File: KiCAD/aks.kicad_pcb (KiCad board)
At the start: 2 copper layers, 30 x 35 mm, 40 parts, among them M3 ОтверстиеD3

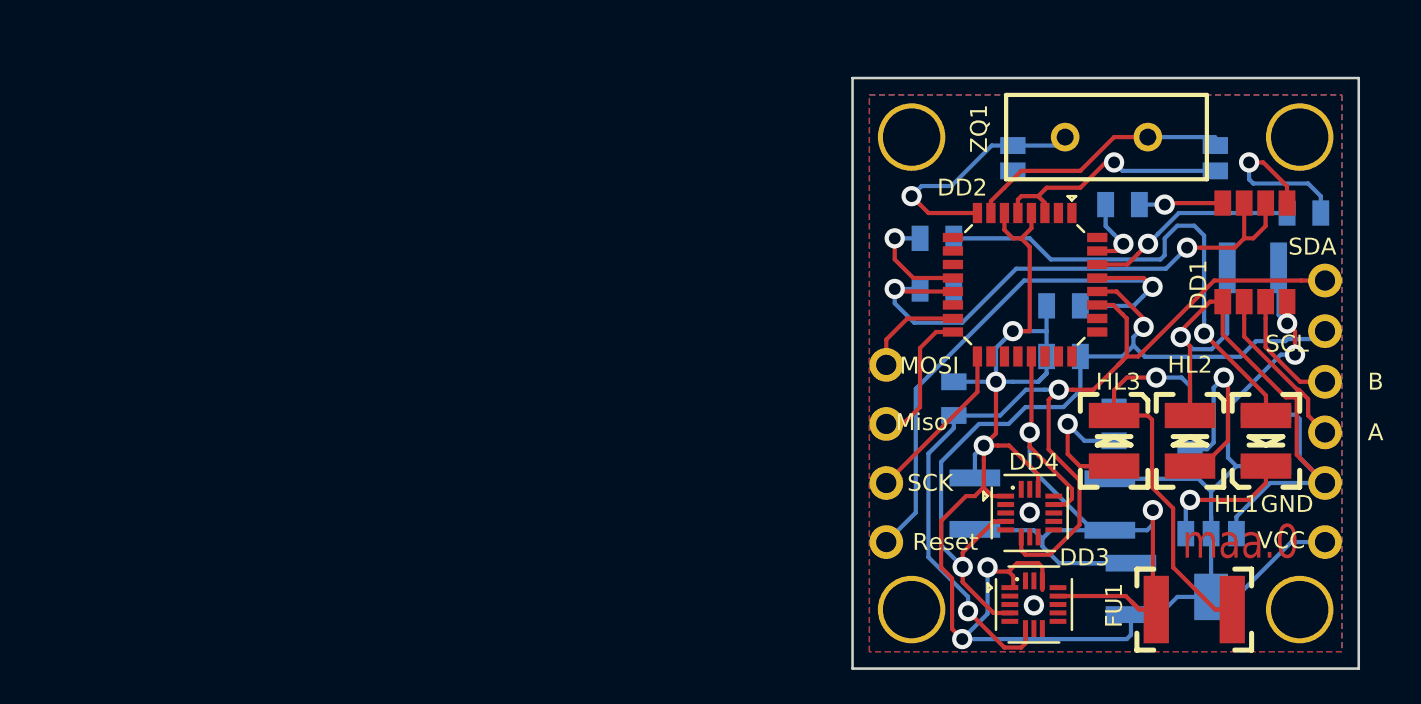
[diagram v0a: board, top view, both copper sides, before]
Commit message: изменен акселерометр
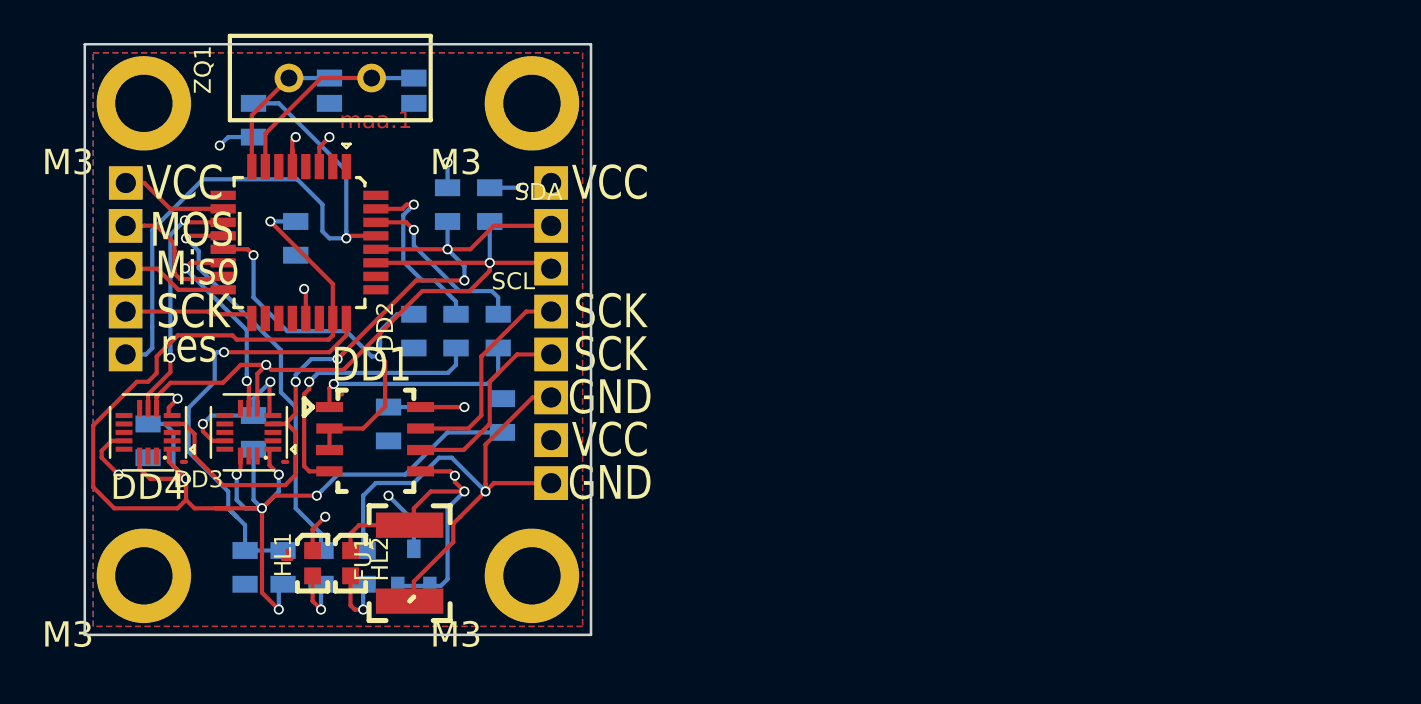
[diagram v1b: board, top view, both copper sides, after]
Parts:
- removed HL3: Светодиод_3Л341Е, MOTOR_VD_VT_HL:Светодиод_SMD_3528
- removed the M3 at (517.5, 292.0)
- removed the M3 at (517.5, 320.0)
- added M3: Отверстие_М3_под_гровер, N_X:Отверстие_М3_под_гровер, F.Cu at (472.0, 318.0)
- added M3: Отверстие_М3_под_гровер, N_X:Отверстие_М3_под_гровер, F.Cu at (472.0, 290.0)
- added R10: Резистор_0,125Вт, N_RLC:Резистор_SMD_0805_0,125Вт, B.Cu at (478.0, 316.5)
- added XS11: VCC, MOTOR_ICO:Отверстие_под_пайку_D1.2, F.Cu at (470.9, 294.7)
- added XS12: VCC, MOTOR_ICO:Отверстие_под_пайку_D1.2, F.Cu at (496.1, 294.7)
- added XS13: GND, MOTOR_ICO:Отверстие_под_пайку_D1.2, F.Cu at (496.1, 312.5)
- C3, C4, C5, C6, C7: footprint MOTOR_IMPORT_OTK:конденсатор_1210 -> N_RLC:Конденсатор_SMD_0805
- DD1: footprint MOTOR_IMPORT_OTK:Микросхема_5559ин10(SO-8) -> N_DD:SO-8_RS485_CAN_Milandr_OTK
- DD2: footprint MOTOR_IMPORT_OTK:ATMEGA-8-161AU -> N_DD:микросхема_ATMEGA-8-161AU
- HL1, HL2: footprint MOTOR_VD_VT_HL:Светодиод_SMD_3528 -> N_VD_HL:Светодиод_SMD_0603
- M3 (x2): value ОтверстиеD3 -> Отверстие_М3_под_гровер; footprint motorchik:ОтверстиеD3 -> N_X:Отверстие_М3_под_гровер
- R8: value Р1-8В-0.125-20к -> Резистор_0,125Вт; footprint MOTOR_RLC:Резистор_SMD_0805_0,125Вт -> N_RLC:Резистор_SMD_0805_0,125Вт
- VD1: footprint MOTOR_VD_VT_HL:Диод_2Д663А95(КТ-99-1) -> N_VD_HL:Диод_BAR43CFILM_SOT-23
- XS1, XS2, XS3, XS4, XS5: footprint motorchik:ОтверстиеКрепежноеD1.2 -> MOTOR_ICO:Отверстие_под_пайку_D1.2
- XS6: value A -> SCK; footprint motorchik:ОтверстиеКрепежноеD1.2 -> MOTOR_ICO:Отверстие_под_пайку_D1.2
- XS7: value B -> SCK; footprint motorchik:ОтверстиеКрепежноеD1.2 -> MOTOR_ICO:Отверстие_под_пайку_D1.2
- XS8: value VCC -> res; footprint MOTOR_ICO:Монтажное_отверстие_D2 -> MOTOR_ICO:Отверстие_под_пайку_D1.2
- moved DD1 58.0 mm to (483.0, 308.0), turned to 0 degrees
- moved HL1 57.3 mm to (482.0, 318.0), turned to 90 degrees
- moved C3 53.4 mm to (486.5, 308.0), turned to 270 degrees
- moved C6 52.8 mm to (481.0, 299.0), turned to 90 degrees
- moved DD4 52.5 mm to (472.2, 309.5), turned to 180 degrees
- moved C4 51.2 mm to (478.5, 308.5), turned to 270 degrees
- moved R6 50.4 mm to (478.5, 290.0), turned to 270 degrees
- moved HL2 50.2 mm to (484.2, 318.0)
- moved R8 50.0 mm to (480.2, 318.5)
- moved R9 49.6 mm to (485.0, 316.5)
- moved R1 49.4 mm to (493.0, 304.5), turned to 90 degrees
- moved C5 49.2 mm to (472.2, 311.0)
- moved C1 47.7 mm to (488.0, 290.0)
- moved DD3 47.6 mm to (478.2, 309.5), turned to 180 degrees
- moved VD1 47.3 mm to (488.0, 317.5), turned to 90 degrees
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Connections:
- C3 pad 1: Ucc -> Ep
- C4 pad 2: Ucc -> VCC
- C5 pad 2: Ucc -> VCC
- C6 pad 2: Ucc -> VCC
- C7 pad 2: Ucc -> VCC
- DD1 pad 8: Ucc -> Ep
- DD2 pad 10: Net-(DD2-Pad10) -> EN1
- DD2 pad 11: Net-(DD2-Pad11) -> PD7
- DD2 pad 14: Net-(DD2-Pad14) -> PB2
- DD2 pad 23: Net-(DD2-Pad23) -> VCC
- DD2 pad 4: Ucc -> Ep
- DD2 pad 6: Ucc -> Ep
- DD3 pad 1: Ucc -> VCC
- DD3 pad 14: Ucc -> VCC
- DD3 pad 5: Net-(DD3-Pad5) -> GND
- DD3 pad 7: Net-(DD3-Pad7) -> PB2
- DD4 pad 1: Ucc -> VCC
- DD4 pad 14: Ucc -> VCC
- DD4 pad 5: Net-(DD4-Pad5) -> GND
- DD4 pad 7: Net-(DD4-Pad7) -> PD7
- FU1 pad 2: GND1 -> GND_in
- R4 pad 1: Ucc -> Ep
- R5 pad 1: Ucc -> Ep
- R6 pad 2: Ucc -> Ep
- R8 pad 1: Net-(HL3-Pad1) -> VCC
- R8 pad 2: GND -> Net-(DD2-Pad24)
- R9 pad 1: GND1 -> GND_in
- VD1 pad 2: Ucc -> Ep
- XS1 pad 1: Ucc -> Ep
- XS10 pad 1: SCL -> SDA
- XS2 pad 1: GND -> GND_in
- XS9 pad 1: SDA -> SCL
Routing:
- net Ucc: track 122.9 -> 0.00 mm, vias 7 -> 0
- net VCC: track 0.00 -> 91.4 mm, vias 0 -> 7
- net GND: track 119.8 -> 45.9 mm, vias 5 -> 10
- net GND_in: track 0.00 -> 32.4 mm, vias 0 -> 1
- net Net-(DD2-Pad24): track 0.00 -> 27.0 mm, vias 0 -> 1
- net GND1: track 26.7 -> 0.00 mm, vias 1 -> 0
- net Net-(HL1-Pad1): track 29.2 -> 3.71 mm
- net SDA: track 62.6 -> 40.7 mm
- net HL1: track 6.66 -> 25.1 mm
- net Ep: track 0.00 -> 16.6 mm, vias 0 -> 5
- net PD7: track 0.00 -> 15.4 mm, vias 0 -> 2
- net PB2: track 0.00 -> 12.7 mm, vias 0 -> 2
- net Net-(DD1-Pad4): track 5.48 -> 16.9 mm
- net Net-(HL3-Pad1): track 9.74 -> 0.00 mm, vias 1 -> 0
- net EN: track 34.1 -> 25.3 mm
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- added copper zone on F.Cu, net Ep
- removed copper zone on F.Cu, net GND
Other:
- net class Default: via_dia 1.2 -> 0.6; via_drill 0.7 -> 0.4
- rule via_min_size: 1.2 -> 0.4
- board text added: "maa.1"
- board text removed: "Reset"
- board text removed: "maa.0"
